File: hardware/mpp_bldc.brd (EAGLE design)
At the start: 36.5 x 20.4 mm, 86 parts, among them IC1 XMEGA16A4U, J2 USB-AB-MICROB-2, U1 LM3480IM3-5, U3 MIC5225-3.3, X1 PASSER-07, X2 PASSER-07

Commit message: tidy up
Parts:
- C5, C6, C7: value 100n/25V -> 100n/50V
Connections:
- net +12V renamed +5V_FET_DRIVER
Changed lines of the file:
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@@
 <grid distance="2" unitdist="mil" unit="mil" style="lines" multiple="1" display="yes" altdistance="0.025" altunitdist="inch" altunit="mil"/>
 <layers>
-<layer number="1" name="Top" color="4" fill="1" visible="no" active="yes"/>
-<layer number="2" name="Route3" color="13" fill="1" visible="no" active="yes"/>
+<layer number="1" name="Top" color="4" fill="1" visible="yes" active="yes"/>
+<layer number="2" name="Route3" color="13" fill="1" visible="yes" active="yes"/>
 <layer number="3" name="Route3" color="4" fill="3" visible="no" active="no"/>
 <layer number="4" name="Route4" color="1" fill="4" visible="no" active="no"/>
@@
 <layer number="22" name="bPlace" color="7" fill="1" visible="yes" active="yes"/>
 <layer number="23" name="tOrigins" color="15" fill="1" visible="no" active="yes"/>
-<layer number="24" name="bOrigins" color="15" fill="1" visible="no" active="yes"/>
+<layer number="24" name="bOrigins" color="15" fill="1" visible="yes" active="yes"/>
 <layer number="25" name="tNames" color="7" fill="1" visible="no" active="yes"/>
 <layer number="26" name="bNames" color="7" fill="1" visible="no" active="yes"/>
@@
 <elements>
 <element name="C1" library="rcl" package="C0603" value="4n7/50V" x="3.8608" y="10.1854" smashed="yes" rot="R180"/>
-<element name="C5" library="rcl" package="C0603" value="100n/25V" x="8.0264" y="2.4384" smashed="yes" rot="R270"/>
-<element name="C6" library="rcl" package="C0603" value="100n/25V" x="12.0904" y="2.4384" smashed="yes" rot="R270"/>
-<element name="C7" library="rcl" package="C0603" value="100n/25V" x="14.1224" y="2.4384" smashed="yes" rot="R270"/>
+<element name="C5" library="rcl" package="C0603" value="100n/50V" x="8.0264" y="2.4384" smashed="yes" rot="R270"/>
+<element name="C6" library="rcl" package="C0603" value="100n/50V" x="12.0904" y="2.4384" smashed="yes" rot="R270"/>
+<element name="C7" library="rcl" package="C0603" value="100n/50V" x="14.1224" y="2.4384" smashed="yes" rot="R270"/>
 <element name="IC1" library="atmel" package="MLF44-TH" value="XMEGA16A4U" x="9.8552" y="13.0048" smashed="yes" rot="R180">
 <attribute name="MF" value="" x="9.8552" y="13.0048" size="1.778" layer="27" rot="R180" display="off"/>
@@
 <wire x1="3.4002" y1="11.8906" x2="3.8608" y2="11.43" width="0.1524" layer="16"/>
 </signal>
-<signal name="+12V">
+<signal name="+5V_FET_DRIVER">
 <contactref element="U$6" pad="4"/>
 <contactref element="D3" pad="A"/>

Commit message: added open hardware symbol :)
Signed-off-by: Julian Wingert <julian.wingert@subtilitas.de>
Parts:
- added U$11: (no value), we-symbol:OSHW_2MM
- moved TP9 0.46 mm to (35.0, 17.2)

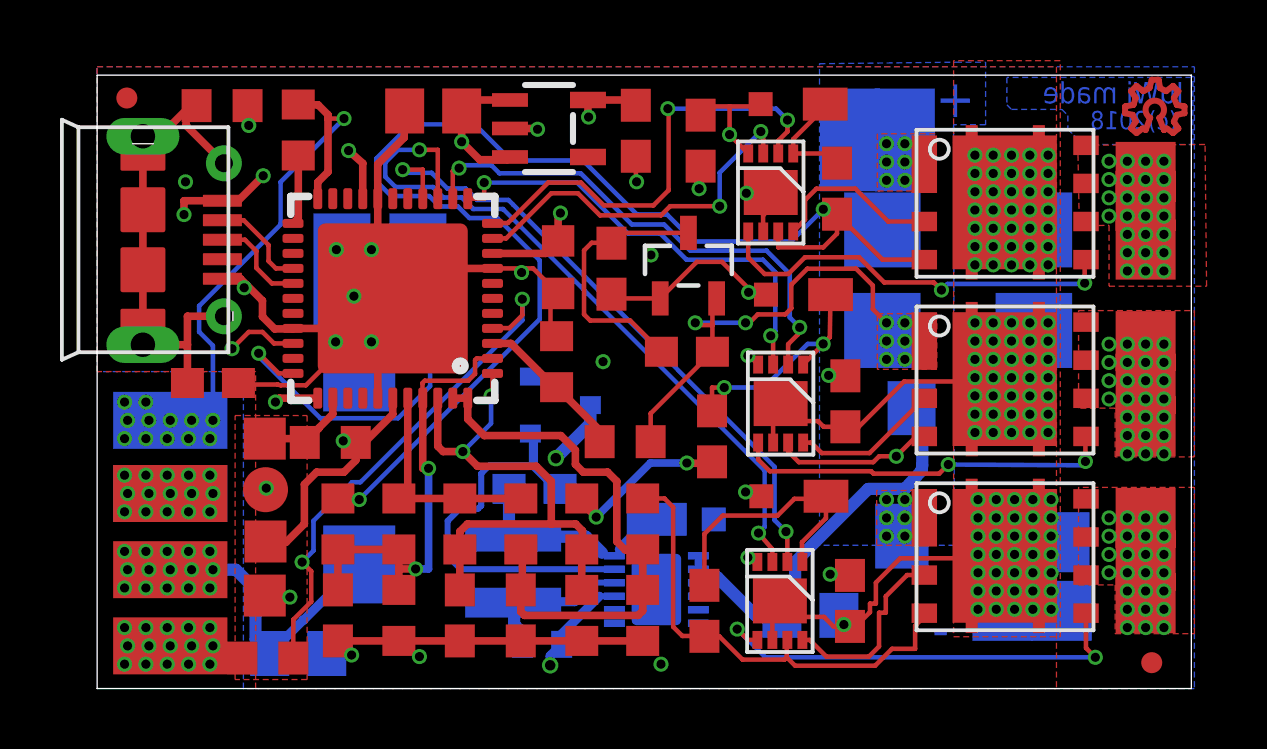
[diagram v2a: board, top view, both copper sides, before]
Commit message: 2.8V Supply for uC reduces power draw further Cleanup and some values (ceramics) reduced to buyable ones
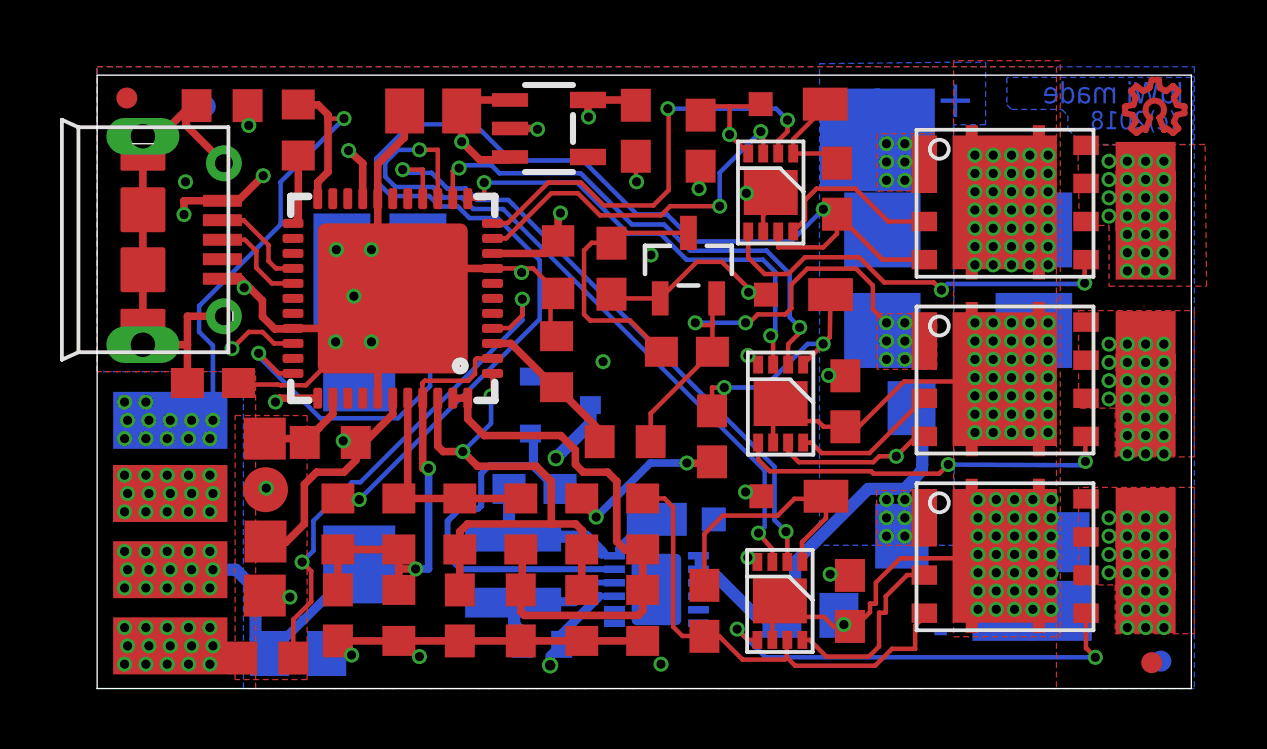
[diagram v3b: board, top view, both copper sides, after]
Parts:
- added X3, X4: PASSER-07, we-symbol:PASSER_07MM
- C19: value 22uF Ceramic 25V -> 10uF Ceramic 25V
- IC1: value XMEGA16A4U -> ATXMEGA16A4U-MH
- R4: value 0.2Ohm -> 0.1Ohm
- U$7: value LT3650-4.2 -> LT3650EDD-4.2#PBF
- U3: value MIC5225-3.3 -> MIC5504-2.8YM5-TR
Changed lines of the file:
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@@
 <?xml version="1.0" encoding="utf-8"?>
 <!DOCTYPE eagle SYSTEM "eagle.dtd">
-<eagle version="9.1.0">
+<eagle version="9.1.3">
 <drawing>
 <settings>
@@
 <element name="C6" library="rcl" package="C0603" value="100n/50V" x="12.0904" y="2.4384" smashed="yes" rot="R270"/>
 <element name="C7" library="rcl" package="C0603" value="100n/50V" x="14.1224" y="2.4384" smashed="yes" rot="R270"/>
-<element name="IC1" library="atmel" package="MLF44-TH" value="XMEGA16A4U" x="9.8552" y="13.0048" smashed="yes" rot="R180">
+<element name="IC1" library="atmel" package="MLF44-TH" value="ATXMEGA16A4U-MH " x="9.8552" y="13.0048" smashed="yes" rot="R180">
 <attribute name="MF" value="" x="9.8552" y="13.0048" size="1.778" layer="27" rot="R180" display="off"/>
 <attribute name="MPN" value="" x="9.8552" y="13.0048" size="1.778" layer="27" rot="R180" display="off"/>
@@
 <element name="C8" library="rcl" package="C0603K" value="10u/10V" x="15.367" y="14.0462" smashed="yes" rot="R90"/>
 <element name="R5" library="rcl" package="R0603" value="4k7" x="7.7724" y="8.2042" smashed="yes" rot="R180"/>
-<element name="U3" library="microbuilder" package="SOT23-5" value="MIC5225-3.3" x="15.0622" y="18.669" smashed="yes" rot="R270"/>
+<element name="U3" library="microbuilder" package="SOT23-5" value="MIC5504-2.8YM5-TR" x="15.0622" y="18.669" smashed="yes" rot="R270"/>
 <element name="C9" library="rcl" package="C0603" value="100n/10V" x="17.9578" y="18.5928" smashed="yes" rot="R270"/>
 <element name="C10" library="rcl" package="C0805" value="10u/10V" x="11.2014" y="19.2532" smashed="yes" rot="R180"/>
@@
 <attribute name="SPICEPREFIX" value="C" x="28.702" y="11.938" size="1.778" layer="28" rot="MR0" display="off"/>
 </element>
-<element name="C19" library="rcl" library_urn="urn:adsk.eagle:library:334" package="C1206" package3d_urn="urn:adsk.eagle:package:23618/2" value="22uF Ceramic 25V" x="28.5496" y="9.3472" smashed="yes" rot="MR180">
+<element name="C19" library="rcl" library_urn="urn:adsk.eagle:library:334" package="C1206" package3d_urn="urn:adsk.eagle:package:23618/2" value="10uF Ceramic 25V" x="28.5496" y="9.3472" smashed="yes" rot="MR180">
 <attribute name="SPICEPREFIX" value="C" x="28.5496" y="9.3472" size="1.778" layer="28" rot="MR180" display="off"/>
 </element>
-<element name="U$7" library="mpp_bldc_ng_2" package="12-WFDFN" value="LT3650-4.2" x="18.6436" y="3.302" smashed="yes" rot="MR270"/>
+<element name="U$7" library="mpp_bldc_ng_2" package="12-WFDFN" value="LT3650EDD-4.2#PBF " x="18.6436" y="3.302" smashed="yes" rot="MR270"/>
 <element name="L1" library="WE-TPC" package="WE-TPC_2828" value=" 732-2617-1-ND " x="13.8684" y="3.9624" smashed="yes" rot="MR0">
 <attribute name="MPN" value="744025001" x="13.8684" y="3.9624" size="1.778" layer="28" rot="MR0" display="off"/>
@@
 </element>
 <element name="C24" library="rcl" package="C0805" value="10uF/25V" x="6.7056" y="1.1684" smashed="yes" rot="MR180"/>
-<element name="R4" library="rcl" package="R0402" value="0.2Ohm" x="14.8336" y="1.4732" smashed="yes" rot="MR180"/>
+<element name="R4" library="rcl" package="R0402" value="0.1Ohm" x="14.8336" y="1.4732" smashed="yes" rot="MR180"/>
 <element name="D5" library="adafruit" library_urn="urn:adsk.eagle:library:420" package="SOT23-R" value="CMPSH1-4" x="15.4432" y="9.4488" smashed="yes" rot="MR90"/>
 <element name="C25" library="rcl" package="C0603" value="1u/25V" x="14.5796" y="6.6548" smashed="yes" rot="MR180"/>
@@
 <element name="D4" library="diode" library_urn="urn:adsk.eagle:library:210" package="SMBJ" package3d_urn="urn:adsk.eagle:package:43442/2" value="SMBJ18A-E3/52GICT-ND" x="28.8544" y="5.08" smashed="yes" rot="MR180"/>
 <element name="U$11" library="we-symbol" package="OSHW_2MM" value="" x="35.2552" y="19.4056"/>
+<element name="X3" library="we-symbol" package="PASSER_07MM" value="PASSER-07" x="35.4584" y="0.9144" rot="MR0"/>
+<element name="X4" library="we-symbol" package="PASSER_07MM" value="PASSER-07" x="3.6068" y="19.4056" rot="MR0"/>
 </elements>
 <signals>

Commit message: to be checked
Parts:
- C10: device rcl:C0805 -> rcl:C0603K
- C9: value 100n/10V -> 100n/25V
- moved C13 4.90 mm to (20.2, 3.38)
- moved C4 4.56 mm to (24.8, 3.15)
- moved C2 4.50 mm to (24.9, 9.47)
- moved C12 4.40 mm to (20.6, 8.71)
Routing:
- net GND: track 87.6 -> 75.6 mm, vias 140 -> 142
- net N$7: track 8.81 -> 3.88 mm
- net N$6: track 7.83 -> 4.27 mm, vias 2 -> 1
- net +5V_FET_DRIVER: track 19.1 -> 21.4 mm, vias 7 -> 5
- net W_HIGH_GATE: track 6.40 -> 5.71 mm
- net V: track 17.9 -> 18.6 mm

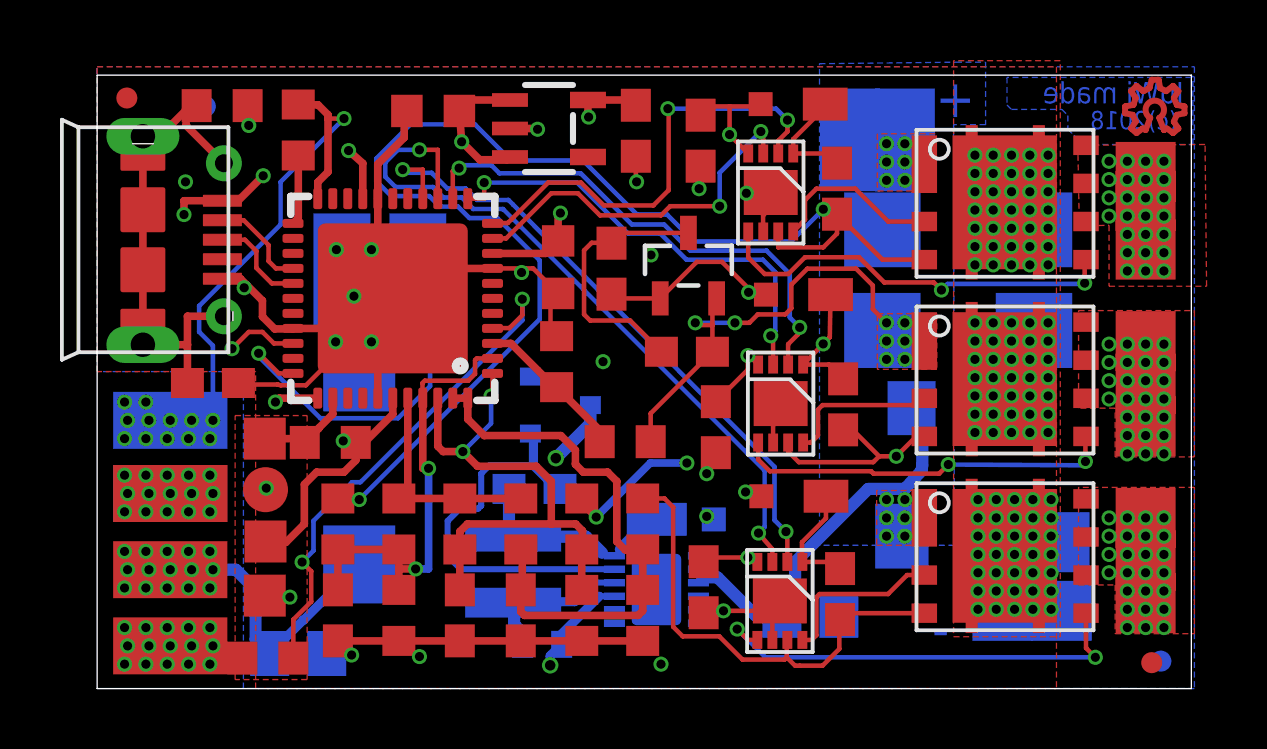
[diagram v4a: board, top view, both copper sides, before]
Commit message: Checked and cleaned up Hardware, repositioned 4 caps
Signed-off-by: Julian Wingert <julian.wingert@subtilitas.de>
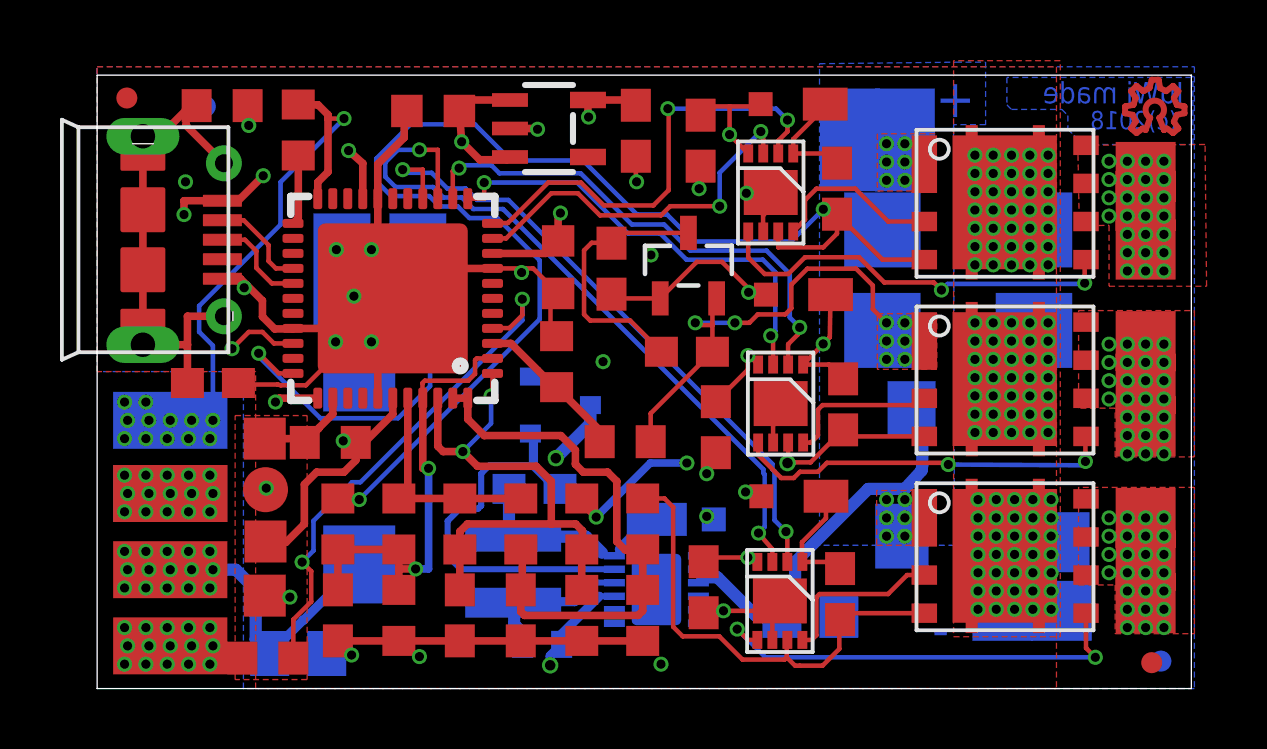
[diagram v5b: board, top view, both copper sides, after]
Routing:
- net V: track 18.6 -> 13.9 mm
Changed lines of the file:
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@@
 <setting verticaltext="up"/>
 </settings>
-<grid distance="2" unitdist="mil" unit="mil" style="lines" multiple="1" display="yes" altdistance="0.025" altunitdist="inch" altunit="mil"/>
+<grid distance="2" unitdist="mil" unit="mil" style="lines" multiple="1" display="no" altdistance="0.025" altunitdist="inch" altunit="mil"/>
 <layers>
 <layer number="1" name="Top" color="4" fill="1" visible="yes" active="yes"/>
@@
 <via x="16.637" y="5.715" extent="1-16" drill="0.3048"/>
 <wire x1="16.637" y1="5.715" x2="18.4404" y2="7.5184" width="0.254" layer="16"/>
-<wire x1="23.0338" y1="7.9034" x2="23.0338" y2="8.1996" width="0.1524" layer="1"/>
-<via x="26.6399" y="7.7423" extent="1-16" drill="0.3048"/>
 <wire x1="18.4404" y1="7.5184" x2="19.6596" y2="7.5184" width="0.254" layer="16"/>
 <via x="19.6596" y="7.5184" extent="1-16" drill="0.3048"/>
-<wire x1="27.5728" y1="8.4052" x2="27.3028" y2="8.4052" width="0.1524" layer="1"/>
-<wire x1="27.3028" y1="8.4052" x2="26.6399" y2="7.7423" width="0.1524" layer="1"/>
-<wire x1="26.6399" y1="7.7423" x2="19.8835" y2="7.7423" width="0.1524" layer="15"/>
-<wire x1="19.8835" y1="7.7423" x2="19.6596" y2="7.5184" width="0.1524" layer="15"/>
-<wire x1="26.0675625" y1="7.7423" x2="25.8714625" y2="7.5462" width="0.1524" layer="1"/>
-<wire x1="25.8714625" y1="7.5462" x2="23.391" y2="7.5462" width="0.1524" layer="1"/>
-<wire x1="23.391" y1="7.5462" x2="23.0338" y2="7.9034" width="0.1524" layer="1"/>
-<wire x1="26.6399" y1="7.7423" x2="26.0675625" y2="7.7423" width="0.1524" layer="1"/>
-<wire x1="24.8666" y1="8.6242" x2="25.1856625" y2="8.6242" width="0.1524" layer="1"/>
-<wire x1="25.1856625" y1="8.6242" x2="26.0675625" y2="7.7423" width="0.1524" layer="1"/>
+<wire x1="19.6596" y1="7.5184" x2="19.8835" y2="7.7423" width="0.1524" layer="15"/>
+<wire x1="19.8835" y1="7.7423" x2="22.7885" y2="7.7423" width="0.1524" layer="15"/>
+<wire x1="22.7885" y1="7.7423" x2="23.0124" y2="7.5184" width="0.1524" layer="15"/>
+<via x="23.0124" y="7.5184" extent="1-16" drill="0.35"/>
+<wire x1="23.0124" y1="7.5184" x2="23.0338" y2="7.5398" width="0.1524" layer="1"/>
+<wire x1="23.0338" y1="7.5398" x2="23.0338" y2="8.1996" width="0.1524" layer="1"/>
+<wire x1="24.8666" y1="8.6242" x2="23.7822" y2="7.5398" width="0.1524" layer="1"/>
+<wire x1="23.7822" y1="7.5398" x2="23.0338" y2="7.5398" width="0.1524" layer="1"/>
+<wire x1="24.8666" y1="8.6242" x2="25.0856" y2="8.4052" width="0.1524" layer="1"/>
+<wire x1="25.0856" y1="8.4052" x2="27.5728" y2="8.4052" width="0.1524" layer="1"/>
 </signal>
 <signal name="W">
@@
 <contactref element="U$2" pad="BG"/>
 <contactref element="U$5" pad="5"/>
-<wire x1="22.0338" y1="7.6334" x2="22.0338" y2="8.1996" width="0.1524" layer="1"/>
 <via x="28.3718" y="7.4676" extent="1-16" drill="0.3048"/>
 <wire x1="28.3718" y1="7.4676" x2="32.8168" y2="7.4422" width="0.1524" layer="16"/>
@@
 <wire x1="32.9438" y1="7.5692" x2="32.9438" y2="8.3862" width="0.1524" layer="1"/>
 <wire x1="32.9438" y1="8.3862" x2="32.9628" y2="8.4052" width="0.1524" layer="1"/>
-<wire x1="22.0338" y1="7.6334" x2="22.4234" y2="7.2438" width="0.1524" layer="1"/>
-<wire x1="28.3718" y1="7.4676" x2="28.0679" y2="7.1637" width="0.1524" layer="1"/>
-<wire x1="25.8" y1="7.2438" x2="22.4234" y2="7.2438" width="0.1524" layer="1"/>
-<wire x1="25.8801" y1="7.1637" x2="25.8" y2="7.2438" width="0.1524" layer="1"/>
-<wire x1="28.0679" y1="7.1637" x2="25.8801" y2="7.1637" width="0.1524" layer="1"/>
+<wire x1="22.80479375" y1="7.0172" x2="23.22000625" y2="7.0172" width="0.1524" layer="1"/>
+<wire x1="22.0338" y1="7.78819375" x2="22.0338" y2="8.1996" width="0.1524" layer="1"/>
+<wire x1="22.80479375" y1="7.0172" x2="22.0338" y2="7.78819375" width="0.1524" layer="1"/>
+<wire x1="23.42910625" y1="7.2263" x2="24.0284" y2="7.2263" width="0.1524" layer="1"/>
+<wire x1="23.22000625" y1="7.0172" x2="23.42910625" y2="7.2263" width="0.1524" layer="1"/>
+<wire x1="24.0284" y1="7.2263" x2="24.32685" y2="7.52475" width="0.1524" layer="1"/>
+<wire x1="24.32685" y1="7.52475" x2="28.31465" y2="7.52475" width="0.1524" layer="1"/>
+<wire x1="28.31465" y1="7.52475" x2="28.3718" y2="7.4676" width="0.1524" layer="1"/>
 </signal>
 <signal name="W_HIGH_GATE">
@@
 <via x="10.7442" y="17.9578" extent="1-16" drill="0.3048"/>
 <wire x1="22.2504" y1="5.3848" x2="22.0472" y2="5.1816" width="0.1524" layer="16"/>
-<wire x1="22.2504" y1="7.2644" x2="22.2504" y2="5.3848" width="0.1524" layer="16"/>
 <wire x1="10.7442" y1="17.9578" x2="10.02753125" y2="17.9578" width="0.1524" layer="16"/>
 <wire x1="10.02753125" y1="17.9578" x2="9.6068" y2="17.53706875" width="0.1524" layer="16"/>
-<wire x1="13.5302" y1="15.9846" x2="22.2504" y2="7.2644" width="0.1524" layer="16"/>
 <wire x1="9.6068" y1="17.53706875" x2="9.6068" y2="17.05773125" width="0.1524" layer="16"/>
 <wire x1="9.6068" y1="17.05773125" x2="9.94573125" y2="16.7188" width="0.1524" layer="16"/>
@@
 <wire x1="11.19446875" y1="16.7188" x2="11.54466875" y2="16.3686" width="0.1524" layer="16"/>
 <wire x1="9.94573125" y1="16.7188" x2="11.19446875" y2="16.7188" width="0.1524" layer="16"/>
+<wire x1="13.5302" y1="15.9846" x2="22.2088" y2="7.306" width="0.1524" layer="16"/>
+<wire x1="22.2088" y1="7.306" x2="22.2088" y2="7.18553125" width="0.1524" layer="16"/>
+<wire x1="22.2088" y1="7.18553125" x2="22.2504" y2="7.14393125" width="0.1524" layer="16"/>
+<wire x1="22.2504" y1="7.14393125" x2="22.2504" y2="5.3848" width="0.1524" layer="16"/>
 </signal>
 <signal name="W_PWM_DRIVE">
@@
 <via x="10.1854" y="17.2974" extent="1-16" drill="0.3048"/>
 <wire x1="22.5806" y1="5.6134" x2="22.9616" y2="5.2324" width="0.1524" layer="16"/>
-<wire x1="22.5806" y1="7.3914" x2="22.5806" y2="5.6134" width="0.1524" layer="16"/>
-<wire x1="13.8684" y1="16.129" x2="22.5806" y2="7.3914" width="0.1524" layer="16"/>
-<wire x1="13.7104" y1="16.287" x2="13.8684" y2="16.129" width="0.1524" layer="16"/>
 <wire x1="12.66353125" y1="16.287" x2="13.7104" y2="16.287" width="0.1524" layer="16"/>
 <wire x1="10.1854" y1="17.2974" x2="10.2908625" y2="17.1919375" width="0.1524" layer="16"/>
@@
 <wire x1="11.66993125" y1="16.671" x2="12.27953125" y2="16.671" width="0.1524" layer="16"/>
 <wire x1="12.27953125" y1="16.671" x2="12.66353125" y2="16.287" width="0.1524" layer="16"/>
+<wire x1="22.5112" y1="7.31079375" x2="22.5806" y2="7.24139375" width="0.1524" layer="16"/>
+<wire x1="22.5806" y1="7.24139375" x2="22.5806" y2="5.6134" width="0.1524" layer="16"/>
+<wire x1="22.5112" y1="7.4862" x2="22.5112" y2="7.31079375" width="0.1524" layer="16"/>
+<wire x1="13.7104" y1="16.287" x2="22.5112" y2="7.4862" width="0.1524" layer="16"/>
 </signal>
 <signal name="+3V3">
